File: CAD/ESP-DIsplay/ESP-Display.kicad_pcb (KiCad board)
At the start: 2 copper layers, 49 parts, among them J101 IO_Conn, J102 Conn_Power, J301 LDO, J302 FTDI_Conn, J601 OLED, J701 Neo, J801 ADC_Conn, SW101 SW_On, SW102 SW_Down, SW103 SW_Up, SW104 SW_T3, SW105 SW_T2, SW106 SW_T1, SW301 Reset, SW302 Flash, SW501 Encoder, U101 SPI-TFT-1-8, U301 LD1117S33TR_SOT223, U302 ESP-12E

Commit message: esp12e adc pinsadded, 1117 power module
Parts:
- J101: footprint Connector_PinHeader_2.54mm:PinHeader_1x04_P2.54mm_Vertical -> Connector_PinHeader_2.54mm:PinHeader_1x08_P2.54mm_Vertical
- J301: value LDO -> Conn_01x03_Female
- moved SW301 29.2 mm to (144.8, 101.6)
- moved SW302 22.9 mm to (121.9, 101.6)
- moved J301 5.08 mm to (168.9, 94.0), turned to 0 degrees
- moved J101 1.27 mm to (91.4, 90.2)
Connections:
- J301 pad 2: GND -> +3V3
- J301 pad 3: +3V3 -> GND
- J601 pad 1: VCC -> +3V3
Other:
- board text added: "3V3"
- board text added: "D C G V"
- board text added: "G C V T R D"
- board text added: "V G A0 D A1 A2 A3 A4"
- board text added: "V S G"
- board text removed: "10..24V"

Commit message: updated schematics
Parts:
- moved R103 33.5 mm to (160.0, 77.5)
- moved D101 25.5 mm to (158.8, 81.3), turned to 0 degrees
- moved D701 25.3 mm to (160.0, 81.3)
- moved C101 8.13 mm to (148.6, 104.1)
- moved SW102 7.62 mm to (156.2, 102.9)
- moved SW103 6.35 mm to (156.2, 90.2)

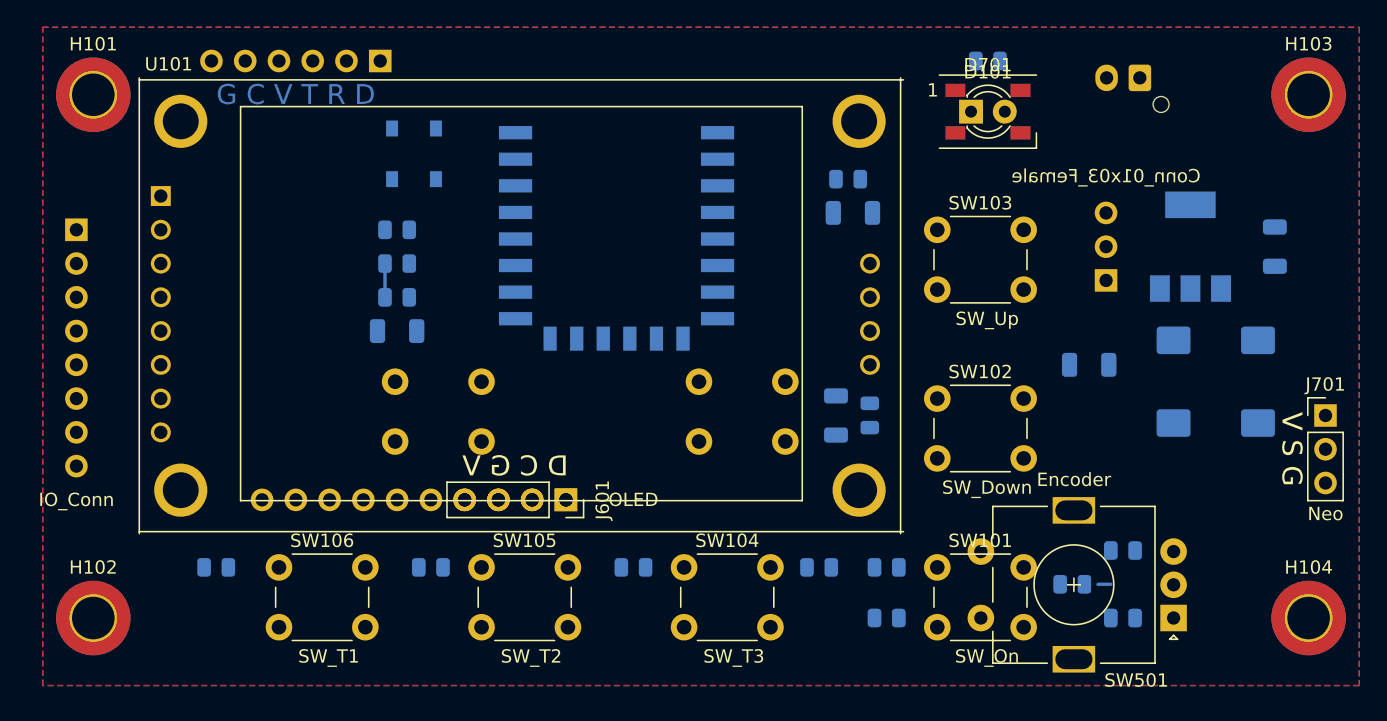
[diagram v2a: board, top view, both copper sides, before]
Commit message: ESP32 added
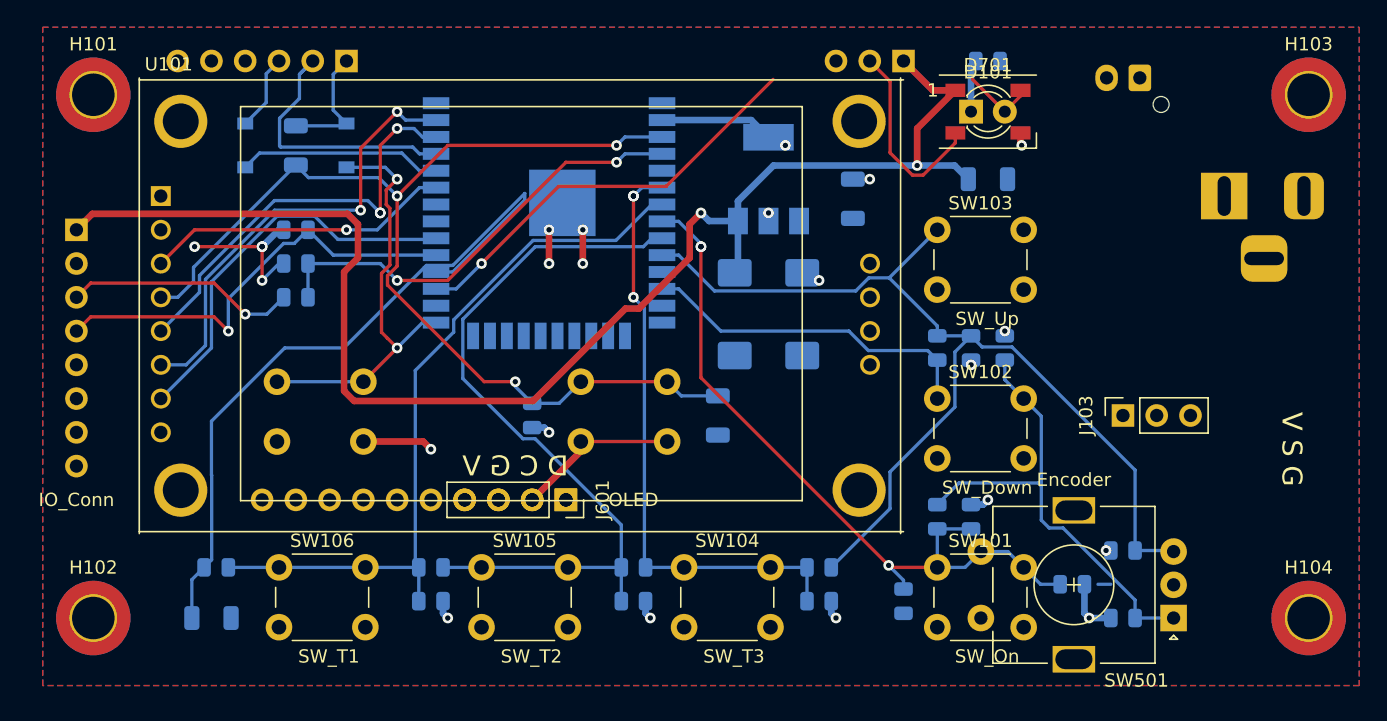
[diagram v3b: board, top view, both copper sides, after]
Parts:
- removed C301, C303: CP, Capacitor_Tantalum_SMD:CP_EIA-7343-15_Kemet-W
- removed C302, C304, C305: C, Capacitor_SMD:C_1206_3216Metric
- removed D301, D302: D_Schottky, Diode_SMD:D_SOD-123
- removed J301: Conn_01x03_Female, Connector_PinSocket_2.54mm:PinSocket_1x03_P2.54mm_Vertical
- removed J302: FTDI_Conn, Connector_PinSocket_2.54mm:PinSocket_1x06_P2.54mm_Vertical
- removed R301: R, Resistor_SMD:R_0805_2012Metric
- removed SW301: Reset, Button_Switch_THT:SW_PUSH_6mm_H5mm
- removed U301: LD1117S33TR_SOT223, Package_TO_SOT_SMD:SOT-223-3_TabPin2
- removed U302: ESP-12E, RF_Module:ESP-12E
- added C102: CP, Capacitor_Tantalum_SMD:CP_EIA-7343-15_Kemet-W, B.Cu at (141.0, 96.5)
- added C103: CP, Capacitor_Tantalum_SMD:CP_EIA-7343-15_Kemet-W, B.Cu at (146.1, 96.5)
- added C104: C, Capacitor_SMD:C_1206_3216Metric, B.Cu at (149.9, 87.8)
- added C105: C, Capacitor_SMD:C_1206_3216Metric, B.Cu at (139.7, 104.1)
- added C106: C, Capacitor_SMD:C_1206_3216Metric, B.Cu at (108.0, 83.8)
- added D102: D_Schottky, Diode_SMD:D_SOD-123, B.Cu at (111.8, 83.8)
- added D103: D_Schottky, Diode_SMD:D_SOD-123, B.Cu at (104.1, 83.8)
- added J103: Conn_01x03_Female, Connector_PinSocket_2.54mm:PinSocket_1x03_P2.54mm_Vertical, F.Cu at (170.2, 104.1)
- added J104: FTDI_Conn, Connector_PinSocket_2.54mm:PinSocket_1x06_P2.54mm_Vertical, B.Cu at (111.8, 77.5)
- added J105: Barrel_Jack_Switch, Connector_BarrelJack:BarrelJack_Horizontal, B.Cu at (177.8, 87.6)
- added R111: R, Resistor_SMD:R_0805_2012Metric, B.Cu at (125.7, 104.1)
- added R401: R, Resistor_SMD:R_0805_2012Metric, B.Cu at (118.1, 118.1)
- added R402: R, Resistor_SMD:R_0805_2012Metric, B.Cu at (133.3, 118.1)
- added R403: R, Resistor_SMD:R_0805_2012Metric, B.Cu at (147.3, 118.1)
- added R404: R, Resistor_SMD:R_0805_2012Metric, B.Cu at (161.3, 99.1)
- added R405: R, Resistor_SMD:R_0805_2012Metric, B.Cu at (158.8, 99.1)
- added R406: R, Resistor_SMD:R_0805_2012Metric, B.Cu at (158.8, 111.8)
- added SW107: Reset, Button_Switch_THT:SW_PUSH_6mm_H5mm, B.Cu at (135.9, 101.6)
- added U102: LD1117S33TR_SOT223, Package_TO_SOT_SMD:SOT-223-3_TabPin2, B.Cu at (143.5, 86.4)
- added U401: ESP32-WROOM-32, RF_Module:ESP32-WROOM-32, B.Cu at (127.0, 88.9)
- J701: moved to B.Cu
- moved C101 49.4 mm to (101.6, 119.4), turned to 180 degrees
- moved J701 41.5 mm to (153.7, 77.5), turned to 90 degrees
- moved C701 15.9 mm to (160.0, 86.4)
- moved SW302 8.89 mm to (113.0, 101.6)
- moved R101 7.62 mm to (108.0, 92.7), turned to 180 degrees
- moved R102 7.62 mm to (108.0, 95.2)
- moved R302 7.62 mm to (108.0, 90.2)
- moved R105 7.18 mm to (156.2, 99.1)
- moved R104 5.39 mm to (156.2, 111.8), turned to 270 degrees
- moved R110 1.80 mm to (153.7, 118.1), turned to 270 degrees
- turned R106 to 180 degrees
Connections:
- net Net-(R106-Pad2) renamed T3
- net Net-(R107-Pad2) renamed T2
- net Net-(R108-Pad2) renamed T1
- R104 pad 1: Net-(R104-Pad1) -> TDN
- R104 pad 2: Net-(R104-Pad2) -> TON
- R105 pad 1: Net-(R104-Pad1) -> TDN
- R105 pad 2: Net-(R105-Pad2) -> TUP
- R106 pad 1: Net-(R105-Pad2) -> TUP
- R110 pad 1: Net-(R104-Pad2) -> TON
- R501 pad 2: ENCB -> TUP
- R502 pad 2: ENCA -> TDN
- R503 pad 2: ENCSW -> TON
- SW101 pad 1: Net-(R104-Pad2) -> TON
- SW102 pad 1: Net-(SW102-Pad1) -> TDN
- SW103 pad 1: Net-(SW103-Pad1) -> TUP
- SW302 pad 1: CS -> GPIO0
- SW501 pad A: ENCA -> TDN
- SW501 pad B: ENCB -> TUP
- SW501 pad S1: ENCSW -> TON
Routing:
- net +5V: track 0.00 -> 108.5 mm, vias 0 -> 2
- net RESET: track 0.00 -> 82.1 mm, vias 0 -> 3
- net TUP: track 0.00 -> 79.4 mm
- net TDN: track 0.00 -> 61.4 mm
- net T2: track 0.00 -> 57.6 mm
- net T1: track 0.00 -> 56.1 mm
- net TON: track 0.00 -> 55.8 mm, vias 0 -> 3
- net READ: track 0.00 -> 55.5 mm
- net T3: track 0.00 -> 45.4 mm, vias 0 -> 3
- net NEO: track 0.00 -> 37.4 mm, vias 0 -> 1
- net GND: track 0.00 -> 35.7 mm, vias 0 -> 10
- net MOSI: track 0.00 -> 34.5 mm, vias 0 -> 2
- net ADC0: track 0.00 -> 33.6 mm, vias 0 -> 2
- net PWM: track 0.00 -> 33.3 mm, vias 0 -> 1
- net GPIO0: track 0.00 -> 31.9 mm, vias 0 -> 2
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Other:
- board text removed: "G C V T R D"

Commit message: ESP Display v1
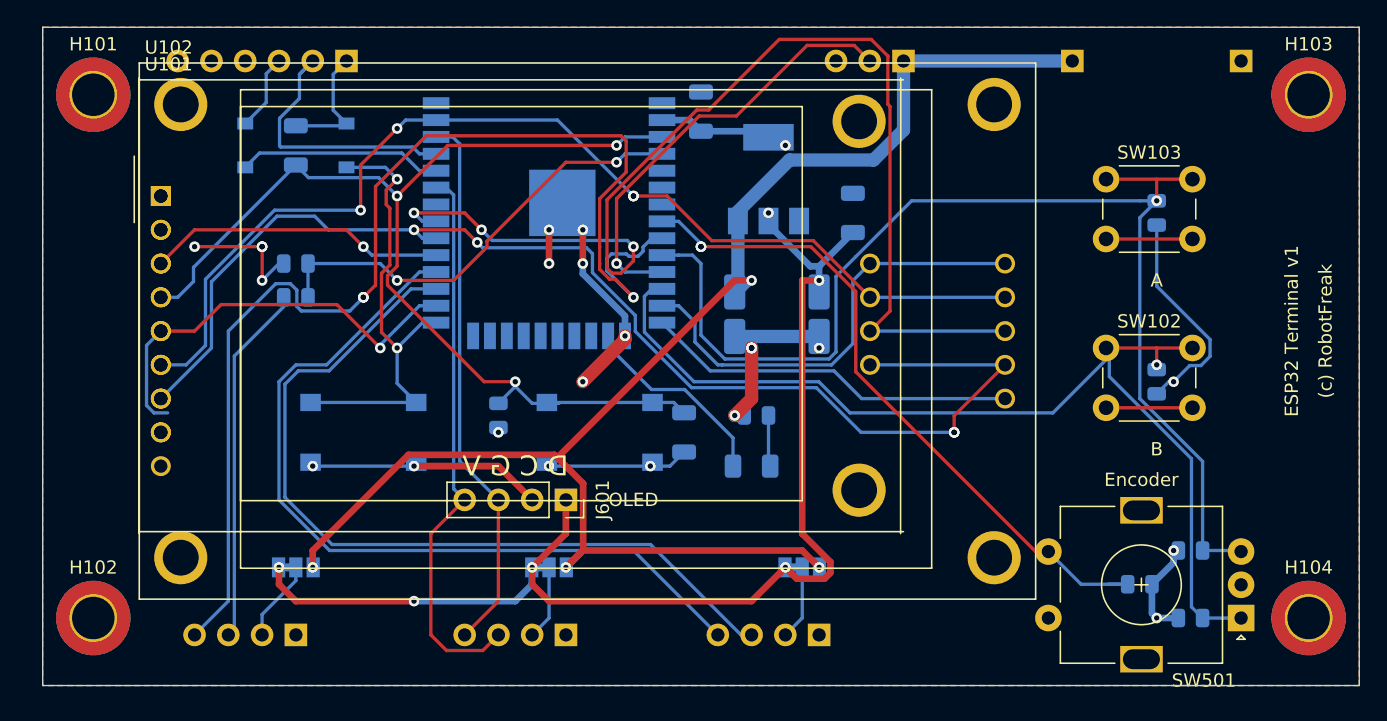
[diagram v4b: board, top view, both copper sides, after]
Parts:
- removed C101, C701: 100nF, Capacitor_SMD:C_1206_3216Metric
- removed C102, C103: CP, Capacitor_Tantalum_SMD:CP_EIA-7343-15_Kemet-W
- removed C104: C, Capacitor_SMD:C_1206_3216Metric
- removed D701: WS2812B, LED_SMD:LED_WS2812B_PLCC4_5.0x5.0mm_P3.2mm
- removed J105: Barrel_Jack_Switch, Connector_BarrelJack:BarrelJack_Horizontal
- removed R104, R109: 47k, Resistor_SMD:R_0805_2012Metric
- removed R105: 33k, Resistor_SMD:R_0805_2012Metric
- removed R106, R107, R108: 22k, Resistor_SMD:R_0805_2012Metric
- removed R110: 1M, Resistor_SMD:R_0805_2012Metric
- removed R302, R401, R402, R403, R406: R, Resistor_SMD:R_0805_2012Metric
- removed SW101: SW_On, Button_Switch_THT:SW_PUSH_6mm_H5mm
- removed SW104: SW_T3, Button_Switch_THT:SW_PUSH_6mm_H5mm
- removed SW105: SW_T2, Button_Switch_THT:SW_PUSH_6mm_H5mm
- removed SW106: SW_T1, Button_Switch_THT:SW_PUSH_6mm_H5mm
- removed SW302: Flash, Button_Switch_THT:SW_PUSH_6mm_H5mm
- added C301: 100nF, Capacitor_SMD:C_1206_3216Metric, B.Cu at (138.4, 81.3)
- added C801: 10µF, Capacitor_SMD:C_Elec_4x5.4, B.Cu at (141.0, 96.5)
- added C802: 10µF, Capacitor_SMD:C_Elec_4x5.4, B.Cu at (147.3, 96.5)
- added C803: 100nF, Capacitor_SMD:C_1206_3216Metric, B.Cu at (149.9, 88.9)
- added J802: VIn-, Connector_PinSocket_2.54mm:PinSocket_1x01_P2.54mm_Vertical, B.Cu at (179.1, 77.5)
- added JP101: PowerJumper, Jumper:SolderJumper-3_P1.3mm_Bridged12_Pad1.0x1.5mm, B.Cu at (108.0, 115.6)
- added JP102: PowerJumper, Jumper:SolderJumper-3_P1.3mm_Bridged12_Pad1.0x1.5mm, B.Cu at (127.0, 115.6)
- added JP103: PowerJumper, Jumper:SolderJumper-3_P1.3mm_Bridged12_Pad1.0x1.5mm, B.Cu at (146.1, 115.6)
- added SW108: SW_Push, Button_Switch_SMD:SW_Push_1P1T_NO_6x6mm_H9.5mm, B.Cu at (113.0, 105.4)
- added U801: LD1117S33TR_SOT223, Package_TO_SOT_SMD:SOT-223-3_TabPin2, B.Cu at (143.5, 86.4)
- D101: footprint LED_THT:LED_D3.0mm_Clear -> LED_SMD:LED_1206_3216Metric; moved to B.Cu
- J101: footprint Connector_PinHeader_2.54mm:PinHeader_1x08_P2.54mm_Vertical -> Connector_PinHeader_2.54mm:PinHeader_1x04_P2.54mm_Vertical
- J102: value Conn_Power -> I2C_Conn; footprint Connector_JST:JST_XH_B2B-XH-AM_1x02_P2.50mm_Vertical -> Connector_PinHeader_2.54mm:PinHeader_1x04_P2.54mm_Vertical
- J103: value Conn_01x03_Female -> UART_Conn; footprint Connector_PinSocket_2.54mm:PinSocket_1x03_P2.54mm_Vertical -> Connector_PinHeader_2.54mm:PinHeader_1x04_P2.54mm_Vertical; moved to B.Cu
- J801: value ADC_Conn -> VIn+; footprint Connector_PinSocket_2.54mm:PinSocket_1x10_P2.54mm_Vertical -> Connector_PinSocket_2.54mm:PinSocket_1x01_P2.54mm_Vertical
- R103: value 1k -> R
- R404, R405: value R -> 10k
- SW107: footprint Button_Switch_THT:SW_PUSH_6mm_H5mm -> Button_Switch_SMD:SW_Push_1P1T_NO_6x6mm_H9.5mm
- U102: value LD1117S33TR_SOT223 -> CR2013-MI2120; footprint Package_TO_SOT_SMD:SOT-223-3_TabPin2 -> Display:CR2013-MI2120; moved to F.Cu
- moved J102 60.2 mm to (128.3, 120.7), turned to 90 degrees
- moved J801 50.4 mm to (166.4, 77.5), turned to 0 degrees
- moved U102 45.7 mm to (97.8, 87.6), turned to 0 degrees
- moved J101 34.7 mm to (108.0, 120.7), turned to 90 degrees
- moved R103 31.9 mm to (142.6, 104.1)
- moved D101 31.4 mm to (142.2, 108.0), turned to 180 degrees
- moved J103 28.2 mm to (147.3, 120.7)
- moved R405 17.3 mm to (172.7, 88.9)
- moved SW102 13.3 mm to (168.9, 99.1)
- moved SW103 13.3 mm to (168.9, 86.4)
- moved R404 11.7 mm to (172.7, 101.6), turned to 90 degrees
- moved SW107 6.35 mm to (130.8, 105.4)
- moved R501 5.08 mm to (175.3, 114.3)
- moved R502 5.08 mm to (175.3, 119.4)
- moved R503 5.08 mm to (171.4, 116.8)
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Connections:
- D101 pad 2: NEO -> LED
- J101 pad 1: +5V -> GND
- J101 pad 2: GND -> Net-(J101-Pad2)
- J102 pad 2: +5V -> Net-(J102-Pad2)
- J103 pad 1: +5V -> GND
- J103 pad 2: +3V3 -> Net-(J103-Pad2)
- J103 pad 3: GND -> RXD2
- J701 pad 2: Net-(D701-Pad2) -> NEO
- J801 pad 1: +3V3 -> +5V
- R103 pad 1: GND -> Net-(D101-Pad1)
- R103 pad 2: Net-(D101-Pad1) -> GND
- U101 pad 10: Net-(U101-Pad10) -> MOSI
- U101 pad 11: Net-(U101-Pad11) -> MISO
- U101 pad 12: Net-(U101-Pad12) -> SCK
- U101 pad 9: Net-(U101-Pad9) -> SD_CS
- U102 pad 1: GND -> +3V3
- U102 pad 2: +3V3 -> GND
- U102 pad 3: +5V -> CS
- U401 pad 11: Net-(U401-Pad11) -> NEO
- U401 pad 13: Net-(U401-Pad13) -> SD_CS
- U401 pad 14: Net-(U401-Pad14) -> FLASH_CD
- U401 pad 16: Net-(U401-Pad16) -> LED
- U401 pad 26: Net-(U401-Pad26) -> DC
- U401 pad 27: NEO -> RXD2
- U401 pad 28: READ -> TXD2
- U401 pad 29: PWM -> CS
- U401 pad 31: Net-(U401-Pad31) -> MISO
- U401 pad 33: CS -> I2C_SDA
- U401 pad 36: DC -> I2C_SCL
- U401 pad 6: T3 -> Net-(U401-Pad6)
- U401 pad 7: T1 -> Net-(U401-Pad7)
- U401 pad 9: T2 -> PWM
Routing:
- net +3V3: track 20.0 -> 121.6 mm, vias 13 -> 11
- net MISO: track 0.00 -> 86.4 mm, vias 0 -> 3
- net SCK: track 30.1 -> 95.4 mm, vias 0 -> 4
- net RXD2: track 0.00 -> 62.3 mm
- net TXD2: track 0.00 -> 61.4 mm
- net T2: track 57.6 -> 0.00 mm
- net PWM: track 33.3 -> 89.6 mm, vias 1 -> 3
- net T1: track 56.1 -> 0.00 mm
- net READ: track 55.5 -> 0.00 mm
- net MOSI: track 34.5 -> 81.9 mm, vias 2 -> 4
- net GND: track 35.7 -> 82.3 mm, vias 10 -> 19
- net T3: track 45.4 -> 0.00 mm, vias 3 -> 0
- net I2C_SDA: track 0.00 -> 42.1 mm
- net I2C_SCL: track 0.00 -> 41.2 mm
- net SD_CS: track 0.00 -> 34.5 mm
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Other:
- board outline added: 99.1 x 49.5 mm
- board text added: "(c) RobotFreak"
- board text added: "+"
- board text added: "-"
- board text added: "13"
- board text added: "16"
- board text added: "17"
- board text added: "18"
- board text added: "21"
- board text added: "22"
- board text added: "23"
- board text added: "25"
- board text added: "26"
- board text added: "27"
- board text added: "32"
- board text added: "33"
- board text added: "36"
- board text added: "4"
- board text added: "5"
- board text added: "A"
- board text added: "B"
- board text added: "C"
- board text added: "CS"
- board text added: "D"
- board text added: "DC"
- board text added: "DC 12"
- board text added: "ESP32 Terminal v1"
- board text added: "FLASH"
- board text added: "FTDI"
- board text added: "G"
- board text added: "I2C"
- board text added: "LED"
- board text added: "MISO"
- board text added: "MISO 19"
- board text added: "MOSI"
- board text added: "MOSI 23"
- board text added: "RESET"
- board text added: "Res"
- board text added: "Rx"
- board text added: "SCK"
- board text added: "SCK 18"
- board text added: "Tx"
- board text added: "UART"
- board text removed: "V G A0 D A1 A2 A3 A4"
- board text removed: "V S G"
- board text removed: "V+"
